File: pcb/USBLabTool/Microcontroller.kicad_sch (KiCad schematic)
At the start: 19 parts, among them J1 Conn_01x06_Pin, J2 Conn_02x12_Odd_Even, SW1 TS02-66-73-BK-100-SCR-D, U12 STM32H562VGTx, Y1 32.768kHz, Y2 NX2016SA-25M-EXS00A-CS08742

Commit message: push new layout
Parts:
- added JP6, JP7: SJ, Jumper:SolderJumper-2_P1.3mm_Open_RoundedPad1.0x1.5mm, symbol Jumper:SolderJumper_2_Open
- added R82, R83: 0, Resistor_SMD:R_0603_1608Metric_Pad0.98x0.95mm_HandSolder, symbol Device:R
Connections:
- net RCC_OSC32_IN: now also R82.2; no longer C35.2, Y1.2
- net RCC_OSC32_OUT: now also R83.2; no longer C36.2, Y1.1
- net RCC_OSC_IN: now also JP6.1 (A); no longer C33.1, Y2.1
- net RCC_OSC_OUT: now also JP7.2 (B); no longer C34.2, Y2.3
- net USB_D+ renamed USB_FN_P
- net USB_D- renamed USB_FN_N
- new net: C36.2, R83.1, Y1.1
- new net: C33.1, JP6.2 (B), Y2.1
- new net: C34.2, JP7.1 (A), Y2.3
- new net: C35.2, R82.1, Y1.2

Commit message: pcb update
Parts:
- added H3, H4: MountingHole, MountingHole:MountingHole_2.2mm_M2, symbol Mechanical:MountingHole

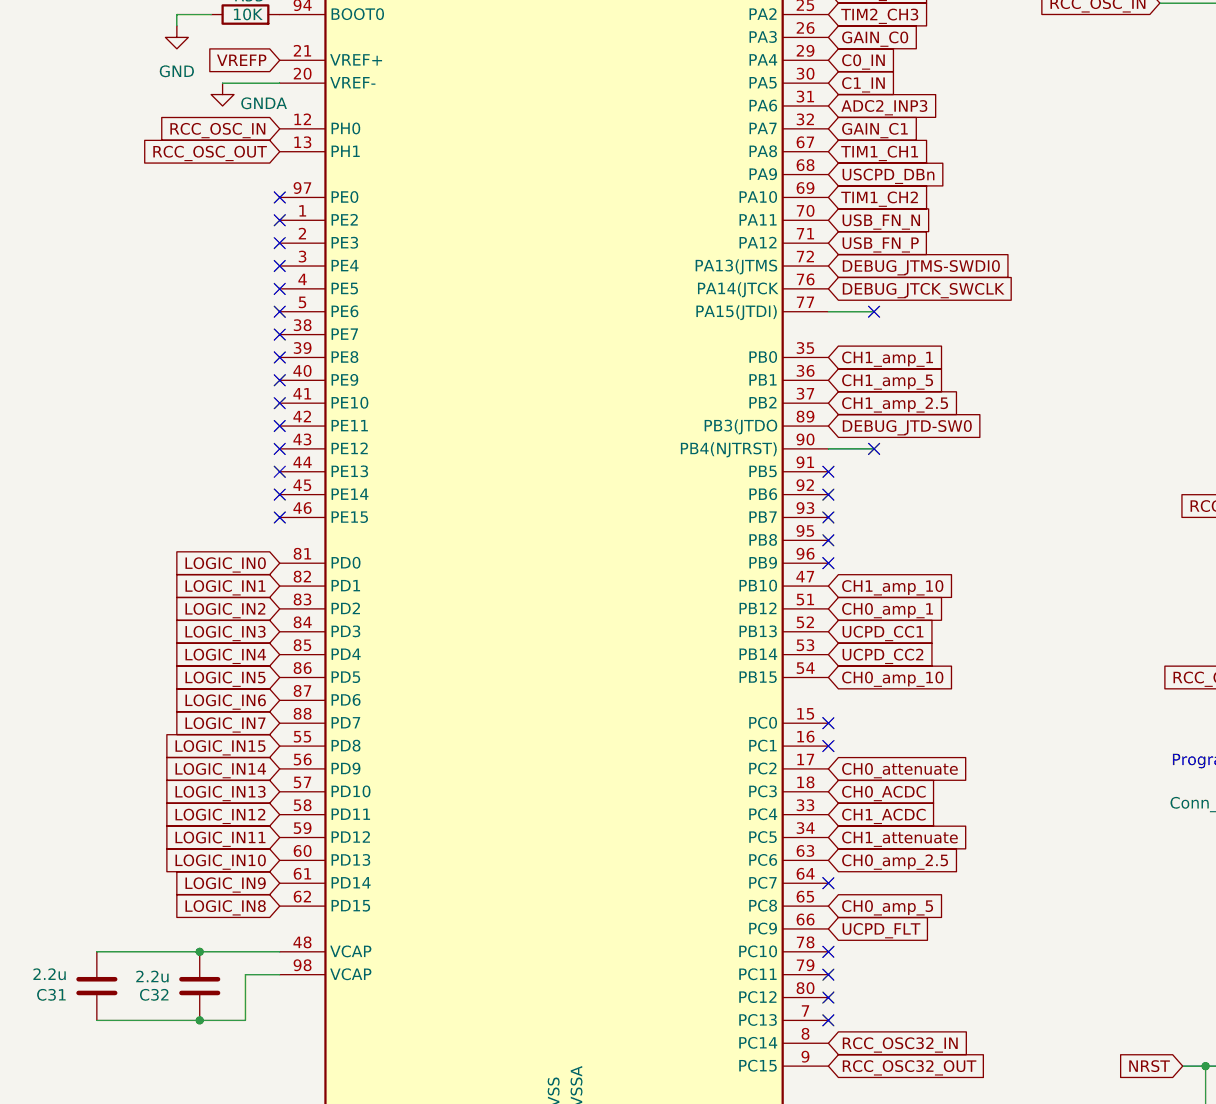
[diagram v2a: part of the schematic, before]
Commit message: change MCU pads and add ground planes and power planes
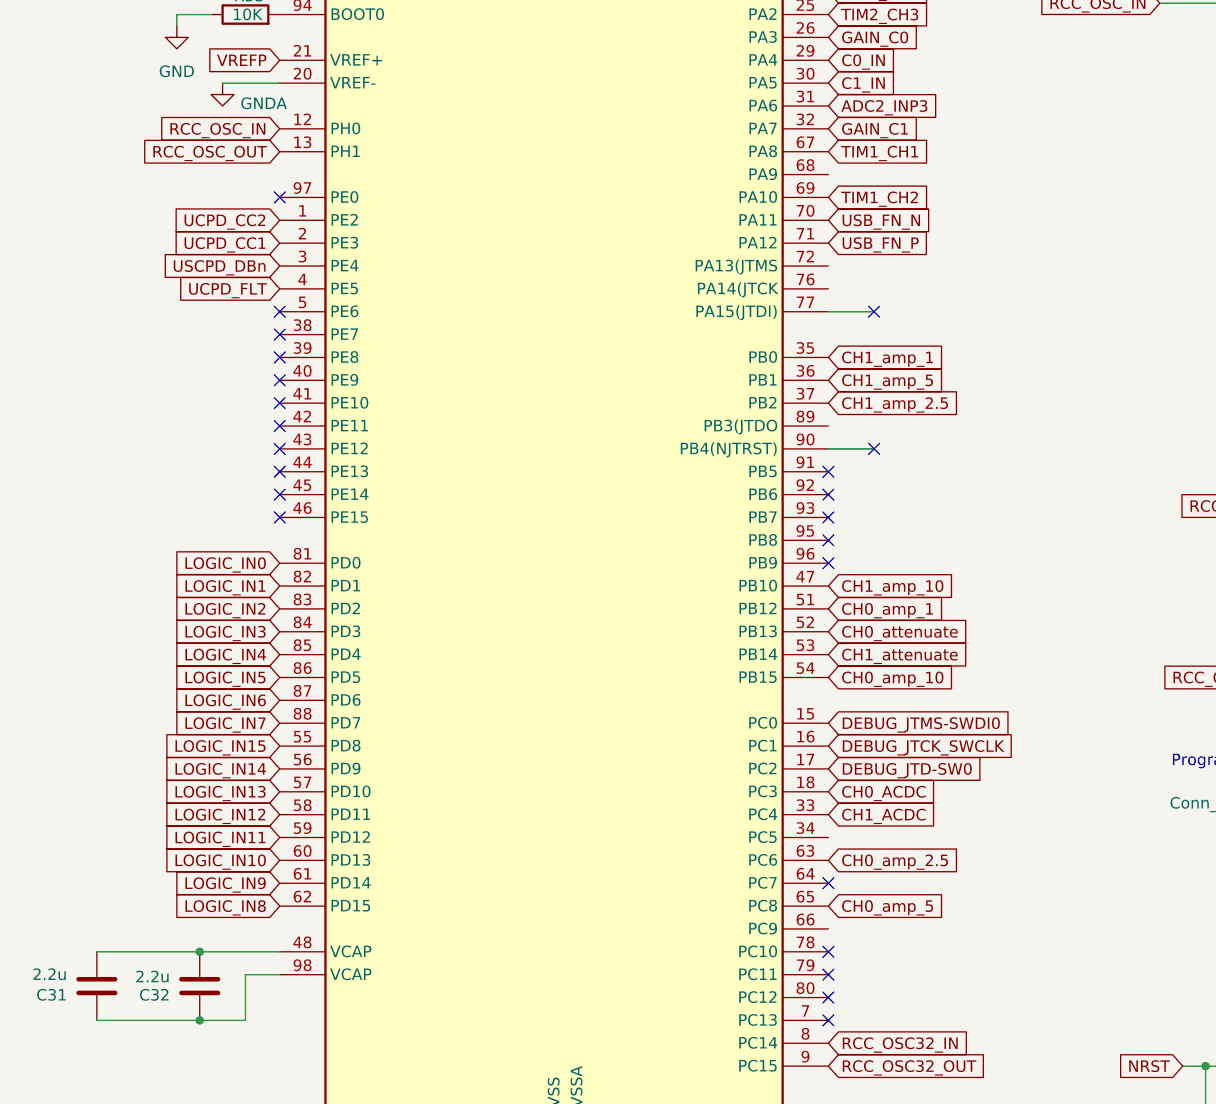
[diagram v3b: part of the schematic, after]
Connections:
- net CH0_attenuate: now also U12.52 (PB13); no longer U12.17 (PC2)
- net CH1_attenuate: now also U12.53 (PB14); no longer U12.34 (PC5)
- net DEBUG_JTCK_SWCLK: now also U12.16 (PC1); no longer U12.76 (PA14(JTCK)
- net DEBUG_JTD-SW0: now also U12.17 (PC2); no longer U12.89 (PB3(JTDO)
- net DEBUG_JTMS-SWDI0: now also U12.15 (PC0); no longer U12.72 (PA13(JTMS)
- net UCPD_CC1: now also U12.2 (PE3); no longer U12.52 (PB13)
- net UCPD_CC2: now also U12.1 (PE2); no longer U12.53 (PB14)
- net UCPD_FLT: now also U12.4 (PE5); no longer U12.66 (PC9)
- net USCPD_DBn: now also U12.3 (PE4); no longer U12.68 (PA9)
- no-connect marks 29 -> 23

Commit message: reposition a few things
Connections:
- net DEBUG_JTCK_SWCLK: now also U12.76 (PA14(JTCK); no longer U12.16 (PC1)
- net DEBUG_JTD-SW0: now also U12.89 (PB3(JTDO); no longer U12.17 (PC2)
- net DEBUG_JTMS-SWDI0: now also U12.72 (PA13(JTMS); no longer U12.15 (PC0)

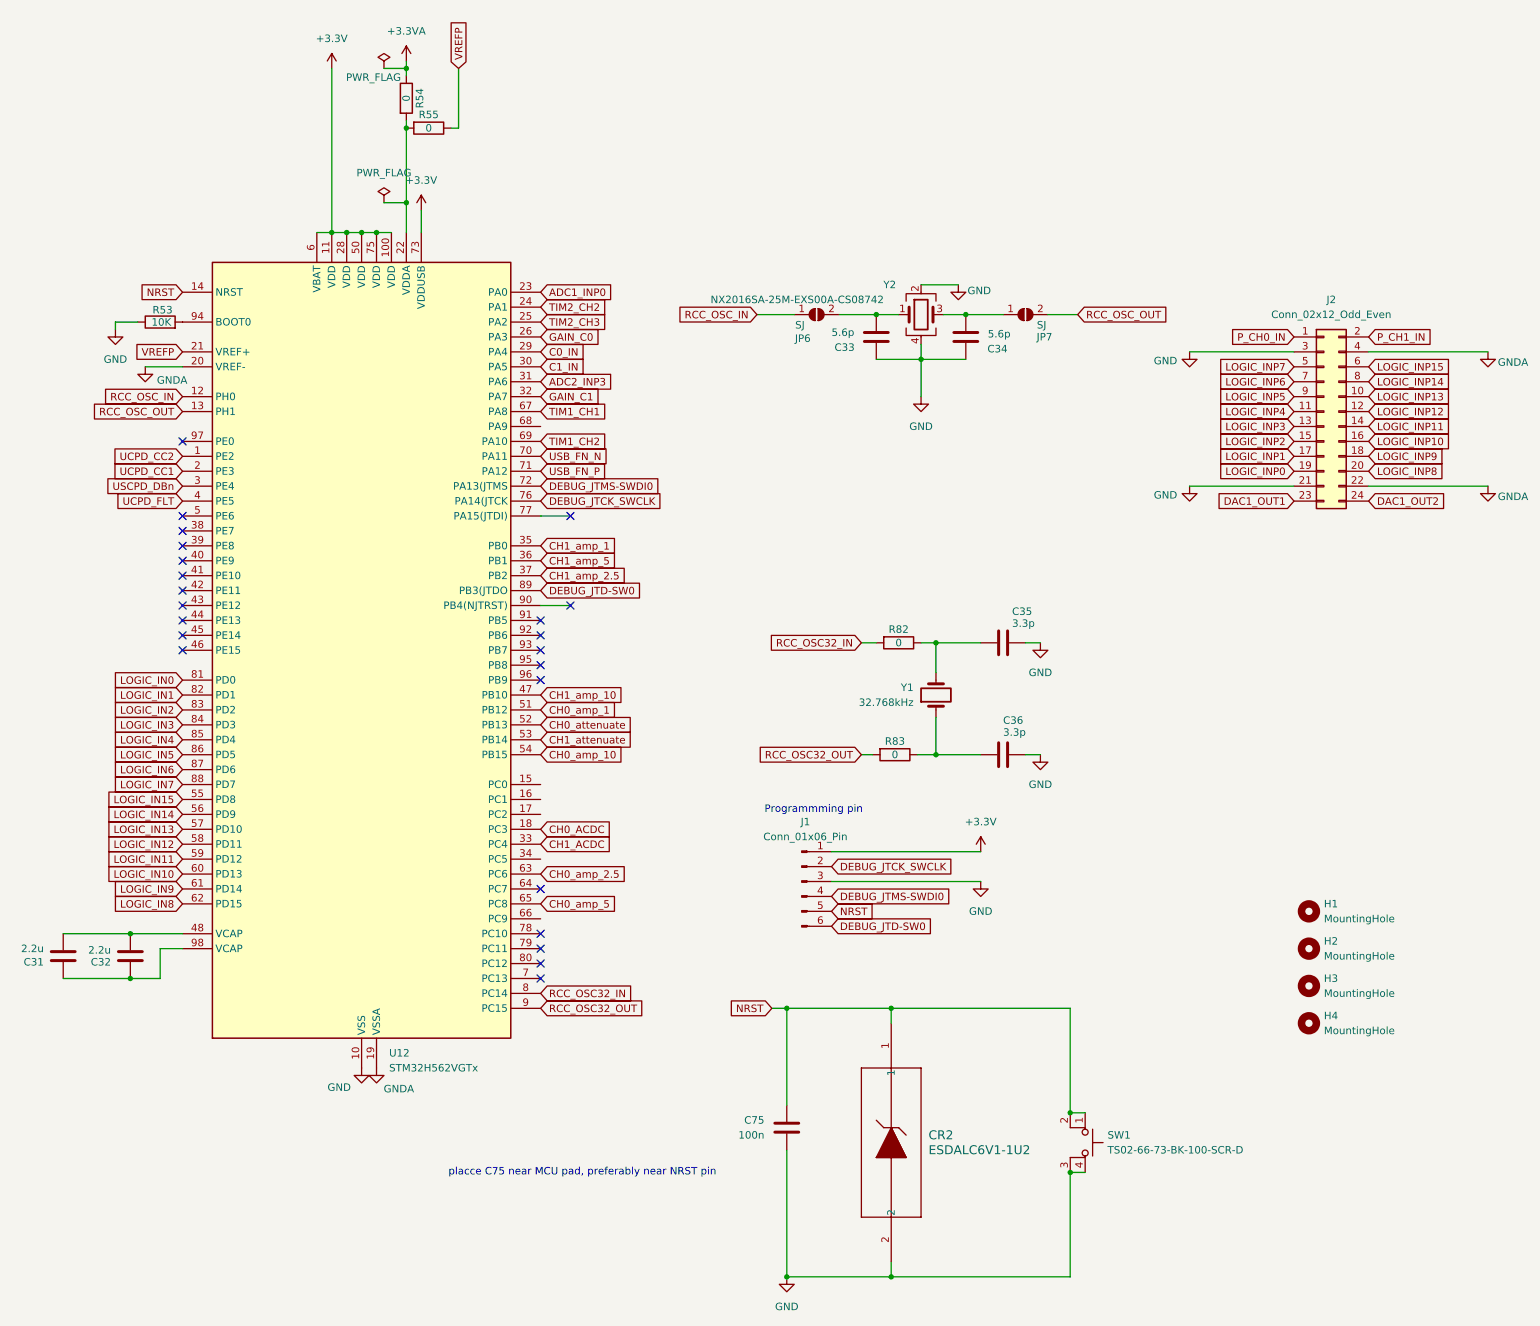
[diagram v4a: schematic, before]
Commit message: nearly finish MCU, need checking, and unfinished logic analyzer
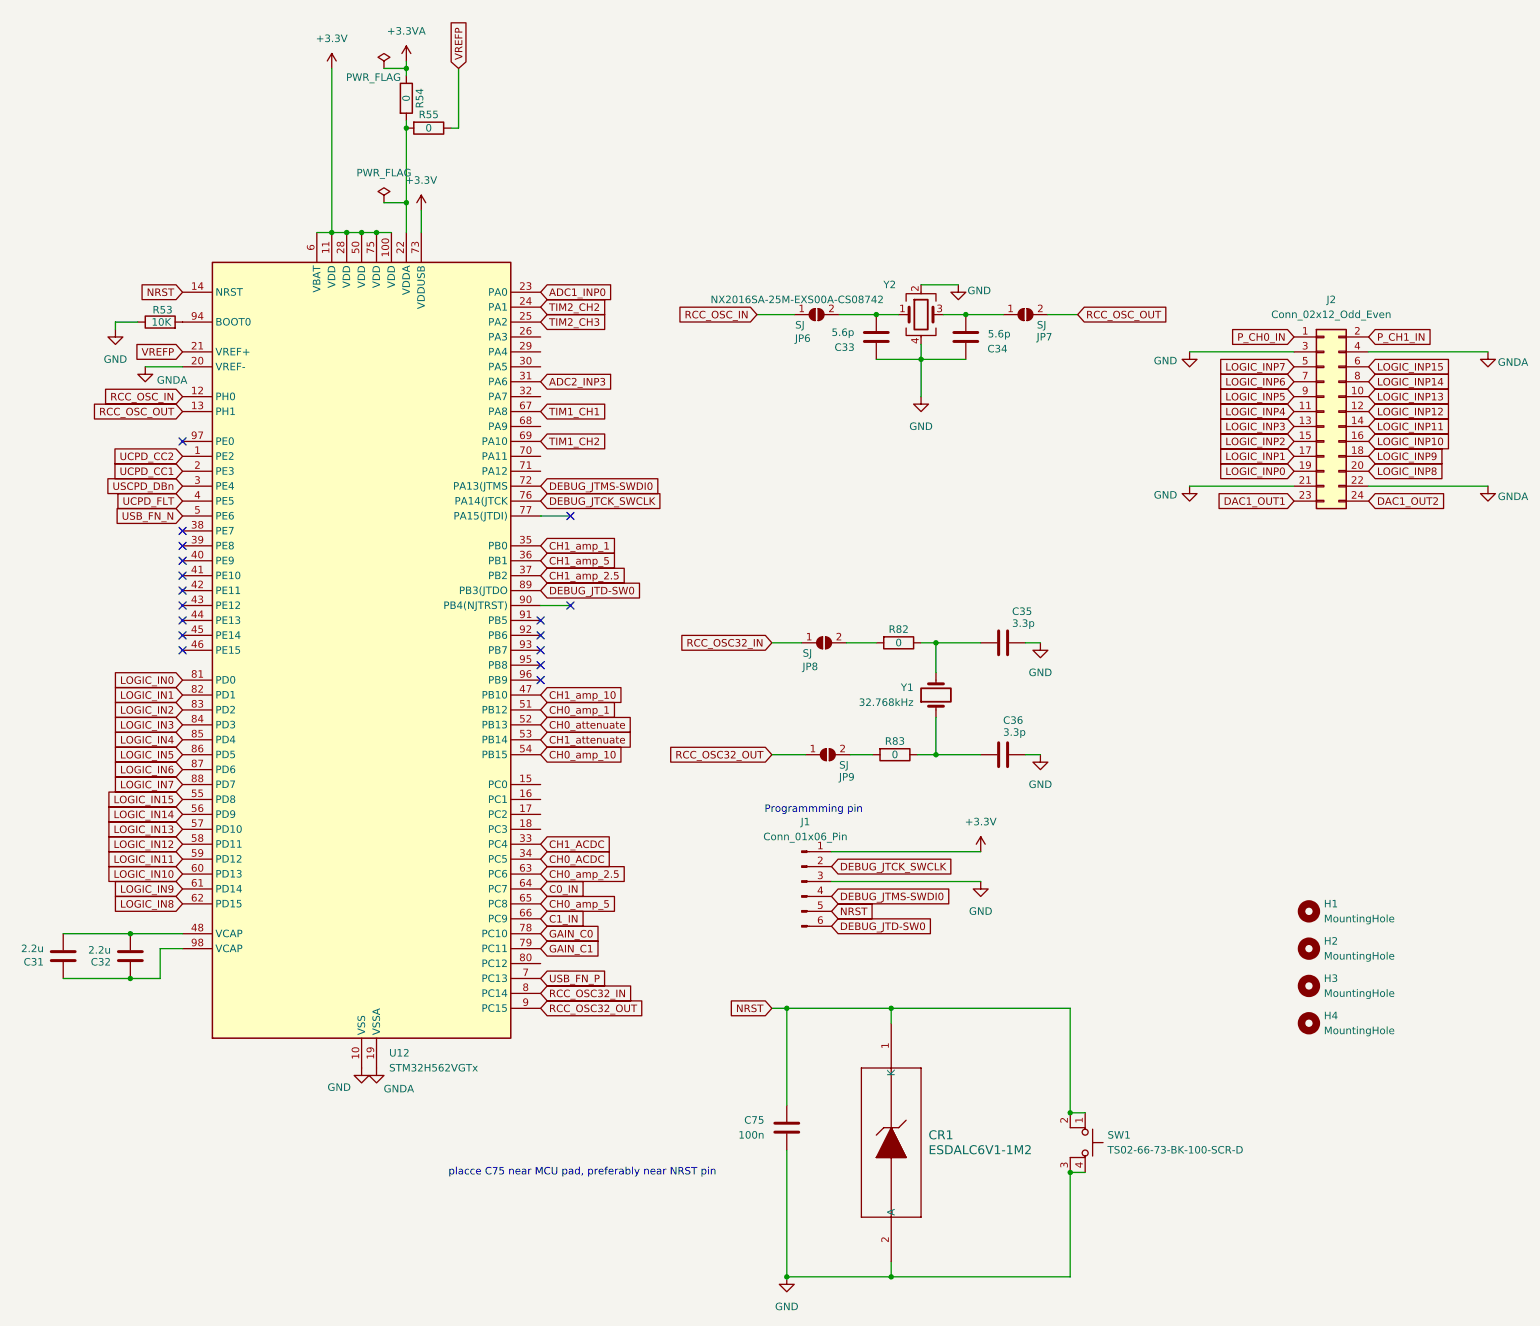
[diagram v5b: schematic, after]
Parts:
- removed CR2: ESDALC6V1-1U2, userfp:DIODE_ESDALC6V1-1U2_STM, symbol USBLabTool:ESDALC6V1-1U2
- added CR1: ESDALC6V1-1M2, SOD882_STM, symbol ESDALC6V1_1M2:ESDALC6V1-1M2
- added JP8, JP9: SJ, Jumper:SolderJumper-2_P1.3mm_Open_RoundedPad1.0x1.5mm, symbol Jumper:SolderJumper_2_Open
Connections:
- net C0_IN: now also U12.64 (PC7); no longer U12.29 (PA4)
- net C1_IN: now also U12.66 (PC9); no longer U12.30 (PA5)
- net CH0_ACDC: now also U12.34 (PC5); no longer U12.18 (PC3)
- net GAIN_C0: now also U12.78 (PC10); no longer U12.26 (PA3)
- net GAIN_C1: now also U12.79 (PC11); no longer U12.32 (PA7)
- net GND: now also CR1.2 (A)
- net NRST: now also CR1.1 (K)
- net RCC_OSC32_IN: now also JP8.1 (A); no longer R82.2
- net RCC_OSC32_OUT: now also JP9.1 (A); no longer R83.2
- net USB_FN_N: now also U12.5 (PE6); no longer U12.70 (PA11)
- net USB_FN_P: now also U12.7 (PC13); no longer U12.71 (PA12)
- new net: JP9.2 (B), R83.2
- new net: JP8.2 (B), R82.2
- no-connect marks 23 -> 17

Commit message: try to do logic analyzer
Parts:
- removed U12: STM32H562VGTx, Package_QFP:LQFP-100_14x14mm_P0.5mm, symbol MCU_ST_STM32H5:STM32H562VGTx
- added U12: STM32H563VITx, Package_QFP:LQFP-100_14x14mm_P0.5mm, symbol MCU_ST_STM32H5:STM32H563VITx
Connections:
- net +3.3V: now also U12.100 (VDD), U12.11 (VDD), U12.28 (VDD), U12.50 (VDD), U12.6 (VBAT), U12.73 (VDDUSB), U12.75 (VDD)
- net ADC1_INP0: now also U12.23 (PA0)
- net ADC2_INP3: now also U12.31 (PA6)
- net C0_IN: now also U12.64 (PC7)
- net C1_IN: now also U12.66 (PC9)
- net CH0_ACDC: now also U12.34 (PC5)
- net CH0_amp_1: now also U12.51 (PB12)
- net CH0_amp_10: now also U12.54 (PB15)
- net CH0_amp_2.5: now also U12.63 (PC6)
- net CH0_amp_5: now also U12.65 (PC8)
- net CH0_attenuate: now also U12.52 (PB13)
- net CH1_ACDC: now also U12.33 (PC4)
- net CH1_amp_1: now also U12.35 (PB0)
- net CH1_amp_10: now also U12.47 (PB10)
- net CH1_amp_2.5: now also U12.37 (PB2)
- net CH1_amp_5: now also U12.36 (PB1)
- net CH1_attenuate: now also U12.53 (PB14)
- net DEBUG_JTCK_SWCLK: now also U12.76 (PA14(JTCK)
- net DEBUG_JTD-SW0: now also U12.89 (PB3(JTDO)
- net DEBUG_JTMS-SWDI0: now also U12.72 (PA13(JTMS)
- net GAIN_C0: now also U12.78 (PC10)
- net GAIN_C1: now also U12.79 (PC11)
- net GND: now also U12.10 (VSS), U12.27 (VSS), U12.49 (VSS), U12.74 (VSS), U12.99 (VSS)
- net GNDA: now also U12.19 (VSSA), U12.20 (VREF-)
- net LOGIC_IN0: now also U12.81 (PD0)
- net LOGIC_IN1: now also U12.82 (PD1)
- net LOGIC_IN10: now also U12.60 (PD13)
- net LOGIC_IN11: now also U12.59 (PD12)
- net LOGIC_IN12: now also U12.58 (PD11)
- net LOGIC_IN13: now also U12.57 (PD10)
- net LOGIC_IN14: now also U12.56 (PD9)
- net LOGIC_IN15: now also U12.55 (PD8)
- net LOGIC_IN2: now also U12.83 (PD2)
- net LOGIC_IN3: now also U12.84 (PD3)
- net LOGIC_IN4: now also U12.85 (PD4)
- net LOGIC_IN5: now also U12.86 (PD5)
- net LOGIC_IN6: now also U12.87 (PD6)
- net LOGIC_IN7: now also U12.88 (PD7)
- net LOGIC_IN8: now also U12.62 (PD15)
- net LOGIC_IN9: now also U12.61 (PD14)
- net NRST: now also U12.14 (NRST)
- net RCC_OSC32_IN: now also U12.8 (PC14)
- net RCC_OSC32_OUT: now also U12.9 (PC15)
- net RCC_OSC_IN: now also U12.12 (PH0)
- net RCC_OSC_OUT: now also U12.13 (PH1)
- net TIM1_CH1: now also U12.67 (PA8)
- net TIM1_CH2: now also U12.69 (PA10)
- net TIM2_CH2: now also U12.24 (PA1)
- net TIM2_CH3: now also U12.25 (PA2)
- net UCPD_CC1: now also U12.2 (PE3)
- net UCPD_CC2: now also U12.1 (PE2)
- net UCPD_FLT: now also U12.4 (PE5)
- net USB_FN_N: now also U12.5 (PE6)
- net USB_FN_P: now also U12.7 (PC13)
- net USCPD_DBn: now also U12.3 (PE4)
- net VREFP: now also U12.21 (VREF+)
- net at C31.1, C32.1: now also U12.98 (VCAP)
- net at C31.2, C32.2: now also U12.48 (VCAP)
- net at R54.2, R55.2: now also U12.22 (VDDA)
- net at R53.2: now also U12.94 (BOOT0)

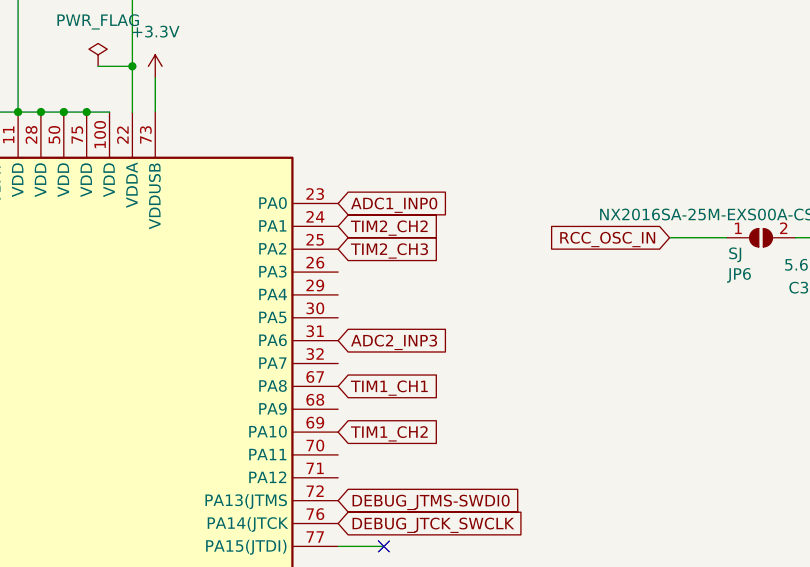
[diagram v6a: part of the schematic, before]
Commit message: clean up layout and create space for logic analyzer
check discord for new MCU pins
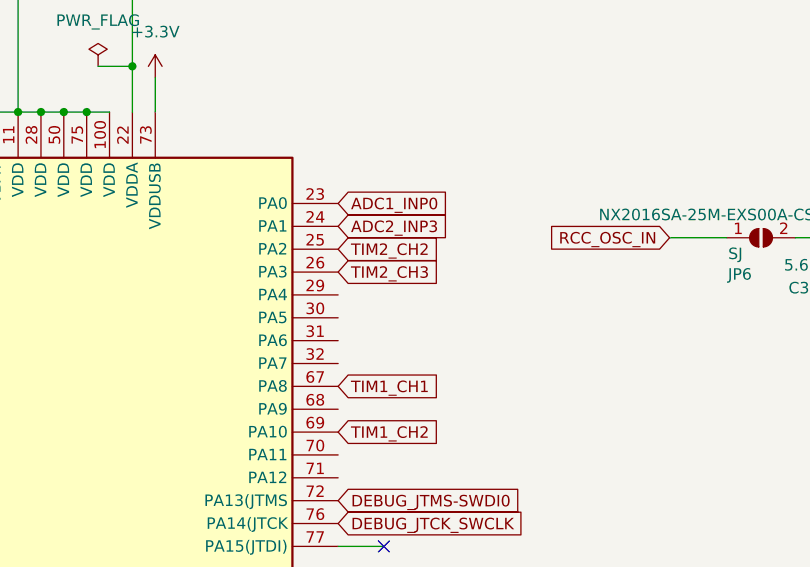
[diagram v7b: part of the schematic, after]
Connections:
- net ADC2_INP3: now also U12.24 (PA1); no longer U12.31 (PA6)
- net TIM2_CH2: now also U12.25 (PA2); no longer U12.24 (PA1)
- net TIM2_CH3: now also U12.26 (PA3); no longer U12.25 (PA2)

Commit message: pcb update
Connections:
- net CH0_attenuate: now also U12.45 (PE14); no longer U12.52 (PB13)
- net CH1_attenuate: now also U12.46 (PE15); no longer U12.53 (PB14)
- net UCPD_CC1: now also U12.52 (PB13); no longer U12.2 (PE3)
- net UCPD_CC2: now also U12.53 (PB14); no longer U12.1 (PE2)
- no-connect marks 17 -> 15
